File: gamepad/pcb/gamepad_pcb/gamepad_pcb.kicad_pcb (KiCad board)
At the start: 2 copper layers, 99 x 99 mm, 9 parts, among them J1 RP CON R, J2 RP CON L, J3 JOYSTICK, SW1 BTN MINUS, SW2 BTN PLUS, SW3 BTN NORTH, SW4 BTN EAST, SW5 BTN SOUTH, SW6 BTN WEST

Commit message: feat: working on pcb
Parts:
- removed J1: RP CON R, Connector_PinSocket_2.54mm:PinSocket_1x20_P2.54mm_Vertical
- removed J2: RP CON L, Connector_PinSocket_2.54mm:PinSocket_1x20_P2.54mm_Vertical
- moved SW4 41.2 mm to (180.2, 92.3)
- moved J3 39.3 mm to (191.1, 67.0)
- moved SW2 35.7 mm to (180.2, 75.2)
- moved SW6 30.4 mm to (180.2, 109.5)
- moved SW3 29.5 mm to (180.2, 83.8)
- moved SW5 28.2 mm to (180.2, 100.9)
- moved SW1 22.6 mm to (180.2, 66.7)
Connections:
- J3 pad 4: Net-(J1-Pin_5) -> +3V3
- J3 pad 5: Net-(J2-Pin_3) -> GND
- SW1 pad 1: Net-(J2-Pin_17) -> GND
- SW1 pad 2: Net-(J2-Pin_3) -> Net-(SW1-Pad2)
- SW2 pad 1: Net-(J2-Pin_19) -> GND
- SW2 pad 2: Net-(J2-Pin_3) -> Net-(U1-GPIO14)
- SW3 pad 1: Net-(J2-Pin_15) -> GND
- SW3 pad 2: Net-(J2-Pin_3) -> Net-(U1-GPIO12)
- SW4 pad 1: Net-(J2-Pin_12) -> GND
- SW4 pad 2: Net-(J2-Pin_3) -> Net-(U1-GPIO10)
- SW5 pad 1: Net-(J2-Pin_14) -> GND
- SW5 pad 2: Net-(J2-Pin_3) -> Net-(U1-GPIO11)
- SW6 pad 1: Net-(J2-Pin_16) -> GND
- SW6 pad 2: Net-(J2-Pin_3) -> Net-(U1-GPIO13)

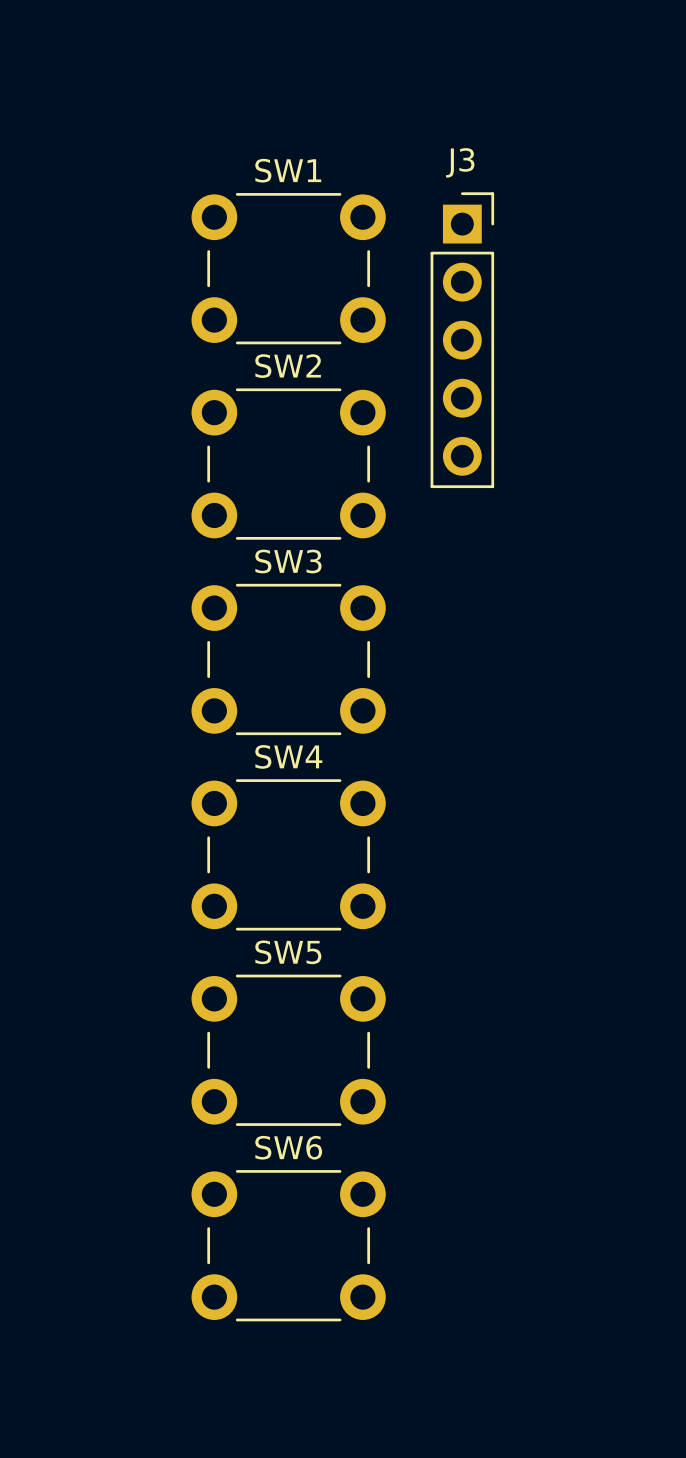
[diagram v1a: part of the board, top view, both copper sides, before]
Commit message: fix: controller schematic
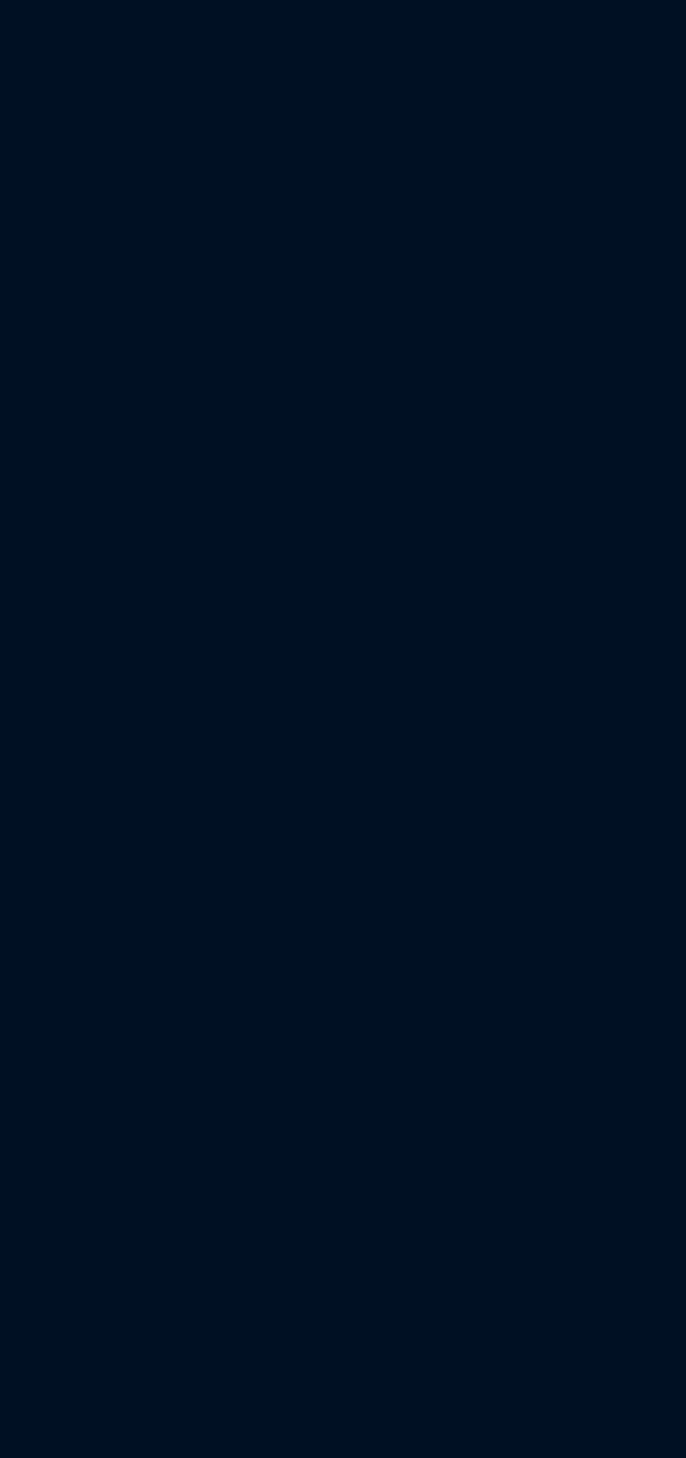
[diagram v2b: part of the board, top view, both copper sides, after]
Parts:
- removed J3: JOYSTICK, Connector_PinSocket_2.54mm:PinSocket_1x05_P2.54mm_Vertical
- removed SW1: BTN MINUS, Button_Switch_THT:SW_PUSH_6mm_H5mm
- removed SW2: BTN PLUS, Button_Switch_THT:SW_PUSH_6mm_H5mm
- removed SW3: BTN NORTH, Button_Switch_THT:SW_PUSH_6mm_H5mm
- removed SW4: BTN EAST, Button_Switch_THT:SW_PUSH_6mm_H5mm
- removed SW5: BTN SOUTH, Button_Switch_THT:SW_PUSH_6mm_H5mm
- removed SW6: BTN WEST, Button_Switch_THT:SW_PUSH_6mm_H5mm
